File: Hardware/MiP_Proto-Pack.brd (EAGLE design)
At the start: 41.4 x 63.8 mm, 5 parts

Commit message: fixed labels
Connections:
- net N$1 renamed 6V
- net N$2 renamed TX
- net N$3 renamed RX
- net N$4 renamed GND
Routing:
- net 6V: track 0.00 -> 5.41 mm
- net GND: track 0.00 -> 5.02 mm
- net TX: track 0.00 -> 4.98 mm
- net RX: track 0.00 -> 4.59 mm
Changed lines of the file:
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@@
 <signal name="N$14">
 </signal>
-<signal name="N$1">
+<signal name="6V">
 <contactref element="JP11" pad="1"/>
 <contactref element="JP1" pad="1"/>
-<wire x1="-12.7" y1="25.4" x2="-17.272" y2="27.432" width="0" layer="19" extent="1-1"/>
+<wire x1="-17.272" y1="27.432" x2="-14.732" y2="27.432" width="1.016" layer="1"/>
+<wire x1="-14.732" y1="27.432" x2="-12.7" y2="25.4" width="1.016" layer="1"/>
 </signal>
-<signal name="N$2">
+<signal name="TX">
 <contactref element="JP11" pad="2"/>
 <contactref element="JP1" pad="2"/>
-<wire x1="-12.7" y1="27.94" x2="-17.272" y2="28.932" width="0" layer="19" extent="1-1"/>
+<wire x1="-17.272" y1="28.932" x2="-13.692" y2="28.932" width="1.016" layer="1"/>
+<wire x1="-13.692" y1="28.932" x2="-12.7" y2="27.94" width="1.016" layer="1"/>
 </signal>
-<signal name="N$3">
+<signal name="RX">
 <contactref element="JP11" pad="3"/>
 <contactref element="JP1" pad="3"/>
-<wire x1="-12.7" y1="30.48" x2="-17.272" y2="30.432" width="0" layer="19" extent="1-1"/>
+<wire x1="-17.272" y1="30.432" x2="-12.748" y2="30.432" width="1.016" layer="1"/>
+<wire x1="-12.748" y1="30.432" x2="-12.7" y2="30.48" width="1.016" layer="1"/>
 </signal>
-<signal name="N$4">
+<signal name="GND">
 <contactref element="JP11" pad="4"/>
 <contactref element="JP1" pad="4"/>
-<wire x1="-12.7" y1="33.02" x2="-17.272" y2="31.932" width="0" layer="19" extent="1-1"/>
+<wire x1="-17.272" y1="31.932" x2="-13.788" y2="31.932" width="1.016" layer="1"/>
+<wire x1="-13.788" y1="31.932" x2="-12.7" y2="33.02" width="1.016" layer="1"/>
 </signal>
 <signal name="N$5">

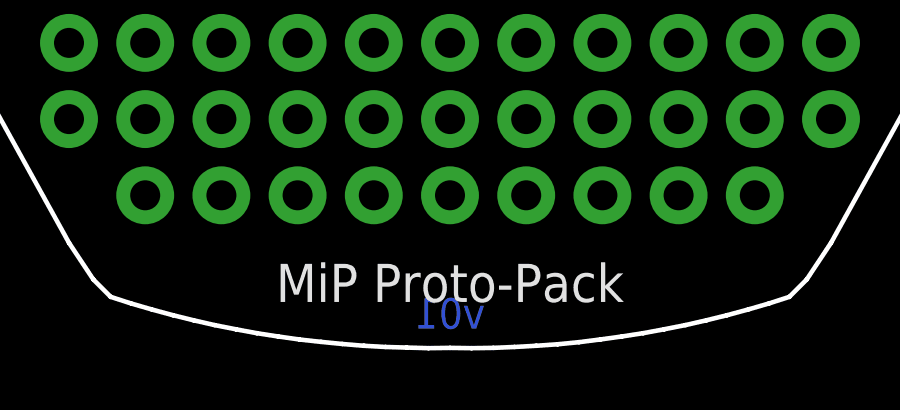
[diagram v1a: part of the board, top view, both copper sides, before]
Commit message: corrected version number, added name to back of PCB
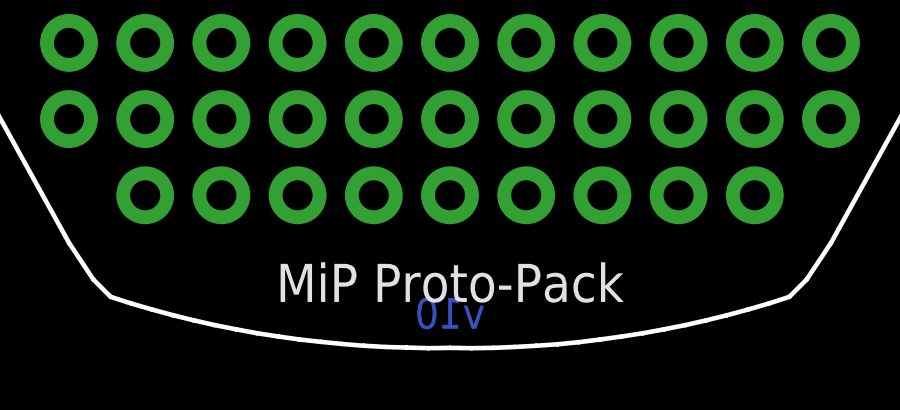
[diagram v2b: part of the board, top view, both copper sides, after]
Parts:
- moved FRAME1 16.5 mm to (-11.4, -10.2)
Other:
- board text added: "v10"
- board text removed: "v01"
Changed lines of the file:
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@@
 <hole x="-14.224" y="21.4376" drill="3.2"/>
 <text x="0" y="2.159" size="1.27" layer="21" font="vector" ratio="15" align="center">MiP Proto-Pack</text>
-<text x="31.75" y="-9.652" size="1.6764" layer="51" ratio="15">Casey Kuhns</text>
-<text x="0" y="1.143" size="1.016" layer="16" font="vector" ratio="15" rot="MR0" align="center">v01</text>
+<text x="19.05" y="-10.16" size="1.6764" layer="51" ratio="15">Casey Kuhns</text>
+<text x="0" y="1.143" size="1.016" layer="16" font="vector" ratio="15" rot="MR0" align="center">v10</text>
 <text x="-15.24" y="32.004" size="0.8128" layer="21" font="vector" ratio="15" align="center">GND</text>
 <text x="-15.494" y="30.48" size="0.8128" layer="21" font="vector" ratio="15" align="center">RX</text>
@@
 <text x="-19.05" y="28.702" size="0.8128" layer="22" font="vector" ratio="15" rot="MR270" align="center">TX</text>
 <text x="-17.272" y="25.146" size="0.8128" layer="22" font="vector" ratio="15" rot="MR0" align="center">6V</text>
+<text x="0" y="2.159" size="1.27" layer="22" font="vector" ratio="15" rot="MR0" align="center">MiP Proto-Pack</text>
 </plain>
 <attributes>
@@
 </autorouter>
 <elements>
-<element name="FRAME1" library="SparkFun-Aesthetics" package="CREATIVE_COMMONS" value="FRAME-LETTER" x="5.0546" y="-9.525"/>
+<element name="FRAME1" library="SparkFun-Aesthetics" package="CREATIVE_COMMONS" value="FRAME-LETTER" x="-11.43" y="-10.16"/>
 <element name="LOGO1" library="SparkFun-Aesthetics" package="SFE_LOGO_NAME_FLAME_.1" value="SFE_LOGO_NAME_FLAME.1_INCH" x="-5.969" y="54.61"/>
 <element name="JP11" library="SparkFun-Connectors" package="1X04-1.5MM_JST" value="" x="-17.272" y="27.432" rot="MR90"/>
